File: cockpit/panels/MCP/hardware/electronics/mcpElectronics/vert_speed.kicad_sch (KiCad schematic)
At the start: 1 part

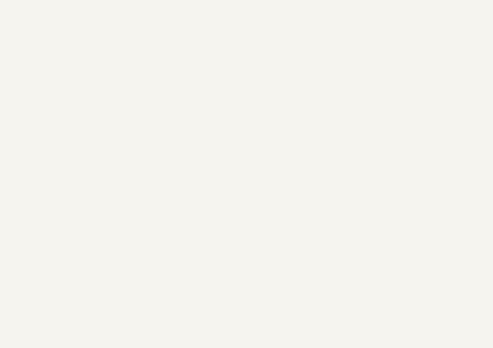
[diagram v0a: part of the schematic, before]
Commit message: update schematic
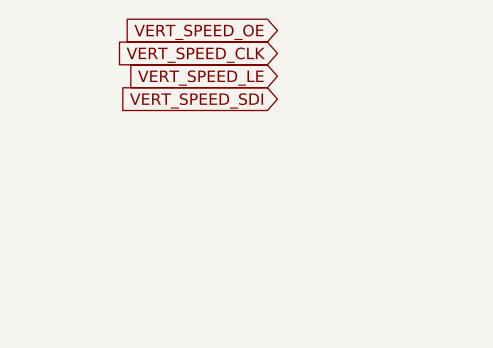
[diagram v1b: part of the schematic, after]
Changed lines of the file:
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@@
     (stroke (width 0) (type default) (color 0 0 0 0))
+  )
+  (global_label "VERT_SPEED_CLK" (shape input) (at 48.26 31.75 180) (fields_autoplaced)
+    (effects (font (size 1.27 1.27)) (justify right))
+    (property "Intersheet References" "${INTERSHEET_REFS}" (id 0) (at 29.8207 31.6706 0)
+      (effects (font (size 1.27 1.27)) (justify right) hide)
+    )
   )
   (global_label "VERT_SPEED_DEC" (shape output) (at 40.64 187.96 180) (fields_autoplaced)
@@
       (effects (font (size 1.27 1.27)) (justify right) hide)
     )
+  )
+  (global_label "VERT_SPEED_OE" (shape input) (at 48.26 29.21 180) (fields_autoplaced)
+    (effects (font (size 1.27 1.27)) (justify right))
+    (property "Intersheet References" "${INTERSHEET_REFS}" (id 0) (at 30.9093 29.1306 0)
+      (effects (font (size 1.27 1.27)) (justify right) hide)
+    )
+  )
+  (global_label "VERT_SPEED_LE" (shape input) (at 48.26 34.29 180) (fields_autoplaced)
+    (effects (font (size 1.27 1.27)) (justify right))
+    (property "Intersheet References" "${INTERSHEET_REFS}" (id 0) (at 31.2117 34.2106 0)
+      (effects (font (size 1.27 1.27)) (justify right) hide)
+    )
+  )
+  (global_label "VERT_SPEED_SDI" (shape input) (at 48.26 36.83 180) (fields_autoplaced)
+    (effects (font (size 1.27 1.27)) (justify right))
+    (property "Intersheet References" "${INTERSHEET_REFS}" (id 0) (at 30.3045 36.7506 0)
+      (effects (font (size 1.27 1.27)) (justify right) hide)
+    )

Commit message: update
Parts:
- added C3, C4 (x4): 100n, Capacitor_SMD:C_0402_1005Metric, symbol Device:C
- added C59: 1u, Capacitor_SMD:C_0402_1005Metric, symbol Device:C
- added J1: WHITE_PLUS_MINUS_LED, Connector_PinHeader_2.54mm:PinHeader_1x05_P2.54mm_Vertical, symbol Connector_Generic:Conn_01x05
- added J18 (x4): WHITE_7_SEGMENT_LED, Connector_PinHeader_2.54mm:PinHeader_1x09_P2.54mm_Vertical, symbol Connector:Conn_01x09_Pin
- added R122: 10k, Resistor_SMD:R_0402_1005Metric, symbol Device:R
- added R138 (x2): 4k7, Resistor_SMD:R_0402_1005Metric, symbol Device:R
- added SW18: V/S, Button_Switch_THT:SW_PUSH_6mm_H5mm, symbol Switch:SW_Push
- SW20: renamed from SW?; footprint (none) -> Rotary_Encoder:RotaryEncoder_Bourns_Vertical_PEC12R-3x17F-Nxxxx
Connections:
- net Earth: now also C3.2, C4.2, C4.2, C4.2, C4.2, C59.2, SW18.1
- net VERT_SPEED_DEC: now also R138.2
- net VERT_SPEED_INC: now also R138.2
- new net +3V3: R122.1, R138.1, R138.1
- new net LEDS_ANODE_17: C4.1, J18.8 (Pin_8), J18.9 (Pin_9)
- new net LEDS_ANODE_18: C4.1, J18.8 (Pin_8), J18.9 (Pin_9)
- new net LEDS_ANODE_19: C4.1, J18.8 (Pin_8), J18.9 (Pin_9)
- new net LEDS_ANODE_20: C4.1, J18.8 (Pin_8), J18.9 (Pin_9)
- new net LEDS_ANODE_21: C3.1, J1.5 (Pin_5)
- new net LEDS_SEGMENTS_ROW_A: J1.1 (Pin_1), J18.1 (Pin_1), J18.1 (Pin_1), J18.1 (Pin_1), J18.1 (Pin_1)
- new net LEDS_SEGMENTS_ROW_B: J1.2 (Pin_2), J18.2 (Pin_2), J18.2 (Pin_2), J18.2 (Pin_2), J18.2 (Pin_2)
- new net LEDS_SEGMENTS_ROW_C: J1.3 (Pin_3), J18.3 (Pin_3), J18.3 (Pin_3), J18.3 (Pin_3), J18.3 (Pin_3)
- new net LEDS_SEGMENTS_ROW_D: J1.4 (Pin_4), J18.4 (Pin_4), J18.4 (Pin_4), J18.4 (Pin_4), J18.4 (Pin_4)
- new net LEDS_SEGMENTS_ROW_E: J18.5 (Pin_5), J18.5 (Pin_5), J18.5 (Pin_5), J18.5 (Pin_5)
- new net LEDS_SEGMENTS_ROW_F: J18.6 (Pin_6), J18.6 (Pin_6), J18.6 (Pin_6), J18.6 (Pin_6)
- new net LEDS_SEGMENTS_ROW_G: J18.7 (Pin_7), J18.7 (Pin_7), J18.7 (Pin_7), J18.7 (Pin_7)
- new net V/S_PUSH: C59.1, R122.2, SW18.2
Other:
- note added: "5 pins required (including CA)"
- note added: "plus/minus display required"
